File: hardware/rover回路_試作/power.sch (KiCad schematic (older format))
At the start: 2 parts

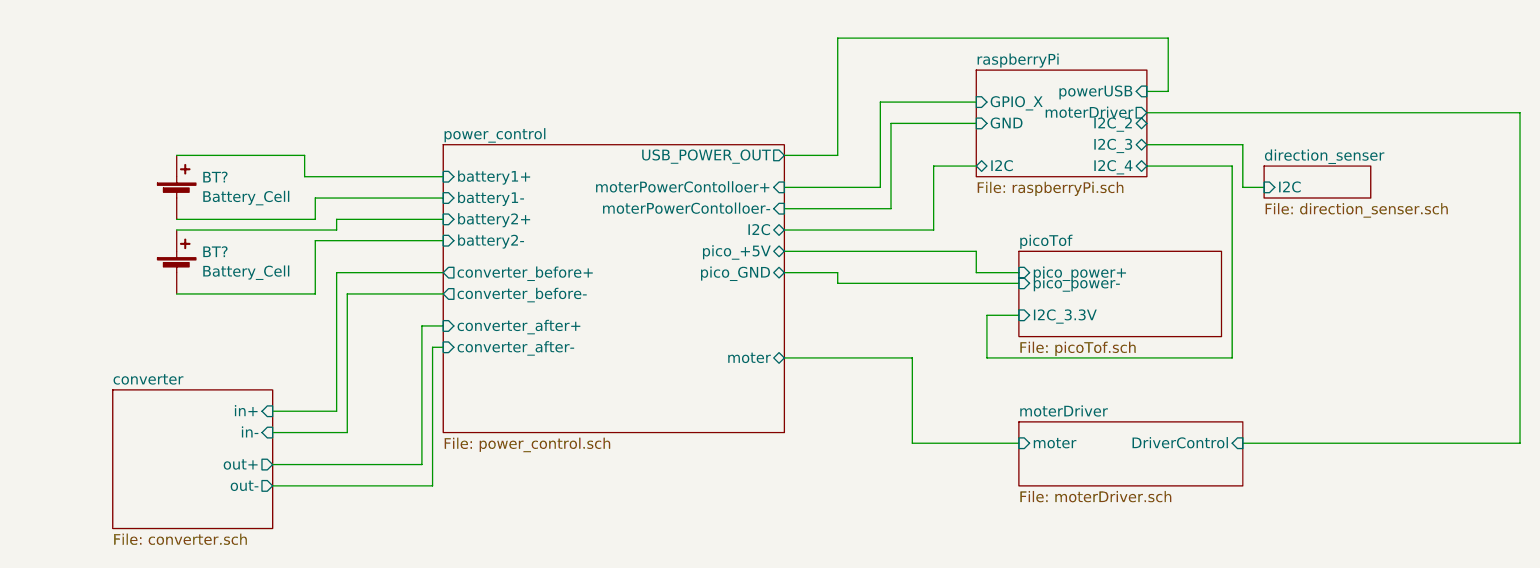
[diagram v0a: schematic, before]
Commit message: rover回路最終版v1.0 降圧回路に関してのみ未記載
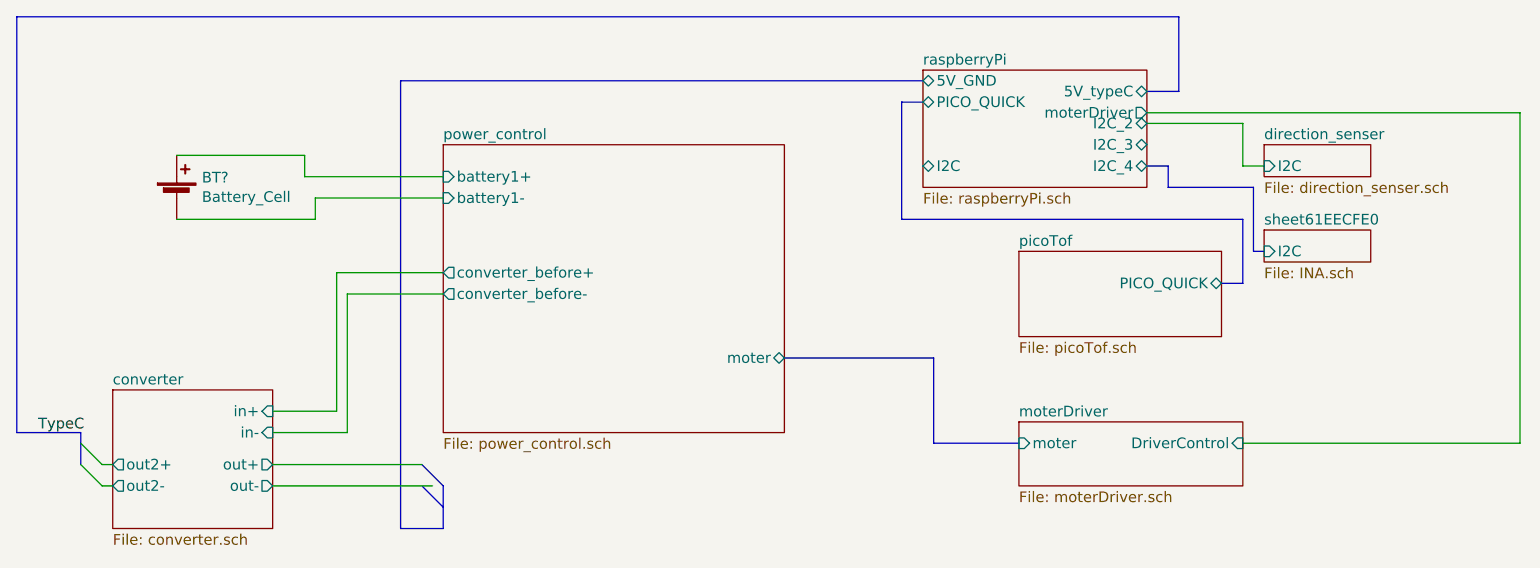
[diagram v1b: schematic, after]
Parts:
- removed BT?: Battery_Cell, symbol Device:Battery_Cell
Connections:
- net labels added: TypeC
- wire segments 58 -> 22
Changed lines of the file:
@@
 $Descr A4 11693 8268
 encoding utf-8
-Sheet 1 7
+Sheet 1 8
 Title ""
 Date ""
@@
 F0 "picoTof" 50
 F1 "picoTof.sch" 50
-F2 "pico_power+" I L 5750 3500 50
-F3 "pico_power-" I L 5750 3550 50
-F4 "I2C_3.3V" I L 5750 3700 50
+F2 "PICO_QUICK" B R 6700 3550 50
 $EndSheet
-Wire Wire Line
-	5750 3550 4900 3550
-Wire Wire Line
-	4900 3550 4900 3500
-Wire Wire Line
-	4900 3500 4650 3500
-Wire Wire Line
-	4650 3400 5550 3400
-Wire Wire Line
-	5550 3400 5550 3500
-Wire Wire Line
-	5550 3500 5750 3500
-$Comp
-L Device:Battery_Cell BT?
-U 1 1 61647480
-P 1800 3150
-F 0 "BT?" H 1918 3246 50  0000 L CNN
-F 1 "Battery_Cell" H 1918 3155 50  0000 L CNN
-F 2 "" V 1800 3210 50  0001 C CNN
-F 3 "~" V 1800 3210 50  0001 C CNN
-	1    1800 3150
-	1    0    0    -1
-$EndComp
-$Comp
-L Device:Battery_Cell BT?
-U 1 1 616480EF
-P 1800 3500
-F 0 "BT?" H 1918 3596 50  0000 L CNN
-F 1 "Battery_Cell" H 1918 3505 50  0000 L CNN
-F 2 "" V 1800 3560 50  0001 C CNN
-F 3 "~" V 1800 3560 50  0001 C CNN
-	1    1800 3500
-	1    0    0    -1
-$EndComp
 Wire Wire Line
 	3050 3050 2400 3050
@@
 	2400 3050 2400 2950
 Wire Wire Line
-	2400 2950 1800 2950
-Wire Wire Line
-	1800 3250 2450 3250
-Wire Wire Line
 	2450 3250 2450 3150
 Wire Wire Line
 	2450 3150 3050 3150
-Wire Wire Line
-	2550 3300 2550 3250
-Wire Wire Line
-	2550 3250 3050 3250
-Wire Wire Line
-	3050 3350 2450 3350
-Wire Wire Line
-	2450 3350 2450 3600
-Wire Wire Line
-	2450 3600 1800 3600
-Wire Wire Line
-	1800 3300 2550 3300
 Wire Wire Line
 	3050 3500 2550 3500
@@
 Wire Wire Line
 	2600 3600 3050 3600
-Wire Wire Line
-	3050 3850 3000 3850
-Wire Wire Line
-	3000 4500 2250 4500
-Wire Wire Line
-	2250 4400 2950 4400
-Wire Wire Line
-	2950 4400 2950 3750
-Wire Wire Line
-	2950 3750 3050 3750
-$Sheet
-S 5550 2550 800  500
-U 6164CA09
-F0 "raspberryPi" 50
-F1 "raspberryPi.sch" 50
-F2 "GND" I L 5550 2800 50
-F3 "GPIO_X" I L 5550 2700 50
-F4 "powerUSB" I R 6350 2650 50
-F5 "I2C" B L 5550 3000 50
-F6 "I2C_2" B R 6350 2800 50
-F7 "I2C_3" B R 6350 2900 50
-F8 "I2C_4" B R 6350 3000 50
-F9 "moterDriver" O R 6350 2750 50
-$EndSheet
-Wire Wire Line
-	6350 2650 6450 2650
-Wire Wire Line
-	6450 2650 6450 2400
-Wire Wire Line
-	4650 3100 5100 3100
-Wire Wire Line
-	5100 3100 5100 2700
-Wire Wire Line
-	5100 2700 5550 2700
-Wire Wire Line
-	5550 2800 5150 2800
-Wire Wire Line
-	5150 2800 5150 3200
-Wire Wire Line
-	5150 3200 4650 3200
-Wire Wire Line
-	5550 3000 5350 3000
-Wire Wire Line
-	5350 3000 5350 3300
-Wire Wire Line
-	5350 3300 4650 3300
-Wire Wire Line
-	3000 3850 3000 4500
-$Sheet
-S 3050 2900 1600 1350
-U 6160D455
-F0 "power_control" 50
-F1 "power_control.sch" 50
-F2 "converter_after+" I L 3050 3750 50
-F3 "converter_after-" I L 3050 3850 50
-F4 "converter_before+" O L 3050 3500 50
-F5 "converter_before-" O L 3050 3600 50
-F6 "moterPowerContolloer+" I R 4650 3100 50
-F7 "moterPowerContolloer-" I R 4650 3200 50
-F8 "battery2+" I L 3050 3250 50
-F9 "battery2-" I L 3050 3350 50
-F10 "battery1+" I L 3050 3050 50
-F11 "battery1-" I L 3050 3150 50
-F12 "pico_+5V" B R 4650 3400 50
-F13 "pico_GND" B R 4650 3500 50
-F14 "I2C" B R 4650 3300 50
-F15 "moter" B R 4650 3900 50
-F16 "USB_POWER_OUT" O R 4650 2950 50
-$EndSheet
 $Sheet
 S 1500 4050 750  650
@@
 F4 "out+" O R 2250 4400 50
 F5 "out-" O R 2250 4500 50
+F6 "out2+" O L 1500 4400 50
+F7 "out2-" O L 1500 4500 50
 $EndSheet
 Wire Wire Line
-	4650 2950 4900 2950
+	6900 3000 6800 3000
 Wire Wire Line
-	4900 2950 4900 2400
+	6800 3000 6800 2800
 Wire Wire Line
-	4900 2400 6450 2400
-Wire Wire Line
-	5750 3700 5600 3700
-Wire Wire Line
-	5600 3700 5600 3900
-Wire Wire Line
-	5600 3900 6750 3900
-Wire Wire Line
-	6750 3900 6750 3000
-Wire Wire Line
-	6750 3000 6350 3000
-$Sheet
-S 6900 3000 500  150
-U 616787AD
-F0 "direction_senser" 50
-F1 "direction_senser.sch" 50
-F2 "I2C" I L 6900 3100 50
-$EndSheet
-Wire Wire Line
-	6900 3100 6800 3100
-Wire Wire Line
-	6800 3100 6800 2900
-Wire Wire Line
-	6800 2900 6350 2900
+	6800 2800 6350 2800
 $Sheet
 S 5750 4200 1050 300
@@
 $EndSheet
 Wire Wire Line
-	4650 3900 5250 3900
-Wire Wire Line
-	5250 3900 5250 4300
-Wire Wire Line
-	5250 4300 5750 4300
-Wire Wire Line
 	6800 4300 8100 4300
 Wire Wire Line
@@
 Wire Wire Line
 	8100 2750 6350 2750
+Wire Wire Line
+	2400 2950 1800 2950
+Wire Wire Line
+	1800 3250 2450 3250
+$Comp
+L Device:Battery_Cell BT?
+U 1 1 61647480
+P 1800 3150
+F 0 "BT?" H 1918 3246 50  0000 L CNN
+F 1 "Battery_Cell" H 1918 3155 50  0000 L CNN
+F 2 "" V 1800 3210 50  0001 C CNN
+F 3 "~" V 1800 3210 50  0001 C CNN
+	1    1800 3150
+	1    0    0    -1
+$EndComp
+$Sheet
+S 3050 2900 1600 1350
+U 6160D455
+F0 "power_control" 50
+F1 "power_control.sch" 50
+F2 "converter_before+" O L 3050 3500 50
+F3 "converter_before-" O L 3050 3600 50
+F4 "battery1+" I L 3050 3050 50
+F5 "battery1-" I L 3050 3150 50
+F6 "moter" B R 4650 3900 50
+$EndSheet
+Wire Wire Line
+	2250 4400 2950 4400
+Wire Bus Line
+	4650 3900 5350 3900
+Wire Bus Line
+	5350 3900 5350 4300
+Wire Bus Line
+	5350 4300 5750 4300
+Entry Wire Line
+	1350 4400 1450 4500
+Entry Wire Line
+	1350 4300 1450 4400
+Wire Wire Line
+	1450 4400 1500 4400
+Wire Wire Line
+	1450 4500 1500 4500
+Wire Bus Line
+	1350 4250 1050 4250
+Text Label 1150 4250 0    50   ~ 0
+TypeC
+Wire Bus Line
+	1050 4250 1050 2300
+Wire Bus Line
+	1050 2300 6500 2300
+Wire Bus Line
+	6500 2300 6500 2650
+Wire Bus Line
+	6350 2650 6500 2650
+$Sheet
+S 5300 2550 1050 550
+U 6164CA09
+F0 "raspberryPi" 50
+F1 "raspberryPi.sch" 50
+F2 "I2C" B L 5300 3000 50
+F3 "I2C_2" B R 6350 2800 50
+F4 "I2C_3" B R 6350 2900 50
+F5 "I2C_4" B R 6350 3000 50
+F6 "moterDriver" O R 6350 2750 50
+F7 "PICO_QUICK" B L 5300 2700 50
+F8 "5V_GND" B L 5300 2600 50
+F9 "5V_typeC" B R 6350 2650 50
+$EndSheet
+Entry Bus Bus
+	2950 4400 3050 4500
+Entry Bus Bus
+	2950 4500 3050 4600
+Wire Bus Line
+	3050 4700 2850 4700
+Wire Bus Line
+	2850 4700 2850 2600
+Wire Bus Line
+	2850 2600 5300 2600
+$Sheet
+S 6900 2900 500  150
+U 616787AD
+F0 "direction_senser" 50
+F1 "direction_senser.sch" 50
+F2 "I2C" I L 6900 3000 50
+$EndSheet
+Wire Bus Line
+	5300 2700 5200 2700
+Wire Bus Line
+	5200 2700 5200 3250
+Wire Bus Line
+	5200 3250 6800 3250
+Wire Bus Line
+	6800 3250 6800 3550
+Wire Bus Line
+	6800 3550 6700 3550
+$Sheet
+S 6900 3300 500  150
+U 61EECFE3
+F0 "sheet61EECFE0" 50
+F1 "INA.sch" 50
+F2 "I2C" I L 6900 3400 50
+$EndSheet
+Wire Bus Line
+	6900 3400 6850 3400
+Wire Bus Line
+	6850 3400 6850 3100
+Wire Bus Line
+	6850 3100 6450 3100
+Wire Bus Line
+	6450 3100 6450 3000
+Wire Bus Line
+	6450 3000 6350 3000
+Wire Bus Line
+	3050 4500 3050 4700
+Wire Wire Line
+	2250 4500 3000 4500
+Wire Bus Line
+	1350 4250 1350 4400
 $EndSCHEMATC
